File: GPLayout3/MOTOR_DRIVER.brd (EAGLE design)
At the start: 162.2 x 45.4 mm, 95 parts, among them T1 2N2222, T2 2N2222, U7 ATMEGA328P_TQFP, Y1 16MHz

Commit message: changed some drill sizes to .8 instead of .6. fixed some clearance issues with LED
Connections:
- removed net THERM2: LED2.THERMAL
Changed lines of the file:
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@@
 <?xml version="1.0" encoding="utf-8"?>
 <!DOCTYPE eagle SYSTEM "eagle.dtd">
-<eagle version="8.0.0">
+<eagle version="8.0.1">
 <drawing>
 <settings>
@@
 <setting verticaltext="up"/>
 </settings>
-<grid distance="6" unitdist="mil" unit="mil" style="lines" multiple="1" display="yes" altdistance="0.05" altunitdist="mm" altunit="mm"/>
+<grid distance="6" unitdist="mil" unit="mm" style="lines" multiple="1" display="yes" altdistance="0.05" altunitdist="mm" altunit="mm"/>
 <layers>
 <layer number="1" name="Top" color="4" fill="1" visible="yes" active="yes"/>
@@
 <wire x1="10.5" y1="25.25" x2="13.25" y2="25.25" width="2" layer="1"/>
 <wire x1="13.25" y1="25.25" x2="14.25" y2="26.25" width="2" layer="1"/>
-<via x="14.25" y="26.25" extent="1-16" drill="0.6"/>
+<via x="14.25" y="26.25" extent="1-16" drill="0.8"/>
 <wire x1="14.25" y1="26.25" x2="16.75" y2="26.25" width="2" layer="16"/>
 <wire x1="16.75" y1="26.25" x2="19.75" y2="29.25" width="2" layer="16"/>
-<via x="19.75" y="29.25" extent="1-16" drill="0.6"/>
+<via x="19.75" y="29.25" extent="1-16" drill="0.8"/>
 <wire x1="19.75" y1="29.25" x2="24.066" y2="29.25" width="2" layer="1"/>
 <wire x1="24.066" y1="29.25" x2="24.536" y2="29.72" width="2" layer="1"/>
@@
 <wire x1="3.166" y1="6.35" x2="3.166" y2="9.166" width="0.3048" layer="16"/>
 <wire x1="3.166" y1="9.166" x2="3.25" y2="9.25" width="0.3048" layer="16"/>
-<via x="3.25" y="9.25" extent="1-16" drill="0.6" diameter="0.6096"/>
+<via x="3.25" y="9.25" extent="1-16" drill="0.8" diameter="0.6096"/>
 <contactref element="SV5" pad="10"/>
 <contactref element="SV5" pad="9"/>
@@
 <contactref element="SV5" pad="7"/>
 <wire x1="3.166" y1="39.55" x2="7.125" y2="39.5" width="2" layer="1"/>
-<via x="7.125" y="39.5" extent="1-16" drill="0.6" shape="square"/>
+<via x="7.125" y="39.5" extent="1-16" drill="0.8" shape="square"/>
 <wire x1="7.125" y1="39.5" x2="29.75" y2="39.5" width="2" layer="16"/>
 <wire x1="29.75" y1="39.5" x2="29.81" y2="42.75" width="2" layer="16"/>
@@
 <wire x1="3.25" y1="22.5" x2="3.25" y2="23" width="2" layer="16"/>
 <wire x1="3.25" y1="23" x2="13.25" y2="23" width="2" layer="16"/>
-<via x="13.25" y="23" extent="1-16" drill="0.6"/>
+<via x="13.25" y="23" extent="1-16" drill="0.8"/>
 <wire x1="15" y1="23" x2="13.25" y2="23" width="2" layer="1"/>
 <wire x1="15.888" y1="23" x2="15" y2="23" width="0.8128" layer="1"/>
@@
 <wire x1="11.258" y1="29.112" x2="7.362" y2="29.112" width="2" layer="1"/>
 <wire x1="7.362" y1="29.112" x2="7.25" y2="29" width="2" layer="1"/>
-<via x="7.25" y="29" extent="1-16" drill="0.6"/>
+<via x="7.25" y="29" extent="1-16" drill="0.8"/>
 <wire x1="7.25" y1="26.252" x2="7.25" y2="29" width="2" layer="16"/>
 <wire x1="17.25" y1="6.25" x2="14.25" y2="6.25" width="0.6096" layer="1"/>
@@
 <wire x1="18.25" y1="25.5" x2="18.25" y2="20.25" width="2" layer="1"/>
 <wire x1="18.25" y1="20.25" x2="19.5" y2="20.25" width="2" layer="1"/>
-<via x="19.5" y="20.25" extent="1-16" drill="0.6"/>
+<via x="19.5" y="20.25" extent="1-16" drill="0.8"/>
 <wire x1="19.5" y1="20.25" x2="25.75" y2="20.25" width="2" layer="16"/>
-<via x="25.75" y="20.25" extent="1-16" drill="0.6"/>
+<via x="25.75" y="20.25" extent="1-16" drill="0.8"/>
 <wire x1="25.75" y1="20.25" x2="25.75" y2="17.594" width="2" layer="1"/>
 <wire x1="25.75" y1="17.594" x2="25.808" y2="17.536" width="2" layer="1"/>
@@
 <vertex x="161.5" y="7.5"/>
 </polygon>
-<contactref element="LED2" pad="THERMAL"/>
 <via x="157.045" y="3.425" extent="1-16" drill="0.381" diameter="0.05" shape="square"/>
 <via x="157.68" y="3.425" extent="1-16" drill="0.381" diameter="0.05" shape="square"/>
@@
 <via x="157.045" y="2.155" extent="1-16" drill="0.381" diameter="0.05" shape="square"/>
 <via x="157.68" y="2.155" extent="1-16" drill="0.381" diameter="0.05" shape="square"/>
-<via x="155.775" y="1.52" extent="1-16" drill="0.381" diameter="0.05" shape="square"/>
-<via x="156.41" y="1.52" extent="1-16" drill="0.381" diameter="0.05" shape="square"/>
+<via x="156.41" y="1.52" extent="1-16" drill="0.381" diameter="0.05"/>
 <via x="157.045" y="1.52" extent="1-16" drill="0.381" diameter="0.05" shape="square"/>
 <via x="157.68" y="1.52" extent="1-16" drill="0.381" diameter="0.05" shape="square"/>
-<via x="158.315" y="1.52" extent="1-16" drill="0.381" diameter="0.05" shape="square"/>
-<via x="158.95" y="1.52" extent="1-16" drill="0.381" diameter="0.05" shape="square"/>
+<via x="158.315" y="1.52" extent="1-16" drill="0.381" diameter="0.05"/>
 <via x="157.045" y="4.06" extent="1-16" drill="0.381" diameter="0.05" shape="square"/>
 <via x="157.68" y="4.06" extent="1-16" drill="0.381" diameter="0.05" shape="square"/>
@@
 <via x="157.68" y="5.33" extent="1-16" drill="0.381" diameter="0.05" shape="square"/>
 <via x="157.045" y="5.965" extent="1-16" drill="0.381" diameter="0.05" shape="square"/>
-<via x="156.41" y="5.965" extent="1-16" drill="0.381" diameter="0.05" shape="square"/>
-<via x="155.775" y="5.965" extent="1-16" drill="0.381" diameter="0.05" shape="square"/>
-<via x="158.315" y="5.965" extent="1-16" drill="0.381" diameter="0.05" shape="square"/>
-<via x="158.95" y="5.965" extent="1-16" drill="0.381" diameter="0.05" shape="square"/>
+<via x="156.41" y="5.965" extent="1-16" drill="0.381" diameter="0.05"/>
+<via x="158.315" y="5.965" extent="1-16" drill="0.381" diameter="0.05"/>
 <via x="157.695" y="5.965" extent="1-16" drill="0.381" diameter="0.05" shape="square"/>
 </signal>
@@
 <vertex x="161.5" y="38"/>
 </polygon>
-<via x="155.775" y="44.015" extent="1-16" drill="0.381" diameter="0.005" shape="square"/>
-<via x="156.41" y="44.015" extent="1-16" drill="0.381" diameter="0.005" shape="square"/>
+<via x="156.41" y="44.015" extent="1-16" drill="0.381" diameter="0.005"/>
 <via x="157.045" y="44.015" extent="1-16" drill="0.381" diameter="0.005" shape="square"/>
 <via x="157.68" y="44.015" extent="1-16" drill="0.381" diameter="0.005" shape="square"/>
-<via x="158.315" y="44.015" extent="1-16" drill="0.381" diameter="0.005" shape="square"/>
-<via x="158.95" y="44.015" extent="1-16" drill="0.381" diameter="0.005" shape="square"/>
+<via x="158.315" y="44.015" extent="1-16" drill="0.381" diameter="0.005"/>
 <via x="157.045" y="43.38" extent="1-16" drill="0.381" diameter="0.005" shape="square"/>
 <via x="157.68" y="43.38" extent="1-16" drill="0.381" diameter="0.005" shape="square"/>
@@
 <via x="157.045" y="40.205" extent="1-16" drill="0.381" diameter="0.005" shape="square"/>
 <via x="157.68" y="40.205" extent="1-16" drill="0.381" diameter="0.005" shape="square"/>
-<via x="155.775" y="39.57" extent="1-16" drill="0.381" diameter="0.005" shape="square"/>
-<via x="156.41" y="39.57" extent="1-16" drill="0.381" diameter="0.005" shape="square"/>
+<via x="156.41" y="39.57" extent="1-16" drill="0.381" diameter="0.005"/>
 <via x="157.045" y="39.57" extent="1-16" drill="0.381" diameter="0.005" shape="square"/>
 <via x="157.68" y="39.57" extent="1-16" drill="0.381" diameter="0.005" shape="square"/>
-<via x="158.315" y="39.57" extent="1-16" drill="0.381" diameter="0.005" shape="square"/>
-<via x="158.95" y="39.57" extent="1-16" drill="0.381" diameter="0.005" shape="square"/>
+<via x="158.315" y="39.57" extent="1-16" drill="0.381" diameter="0.005"/>
 <polygon width="0.4064" layer="1">
 <vertex x="153.5" y="45"/>

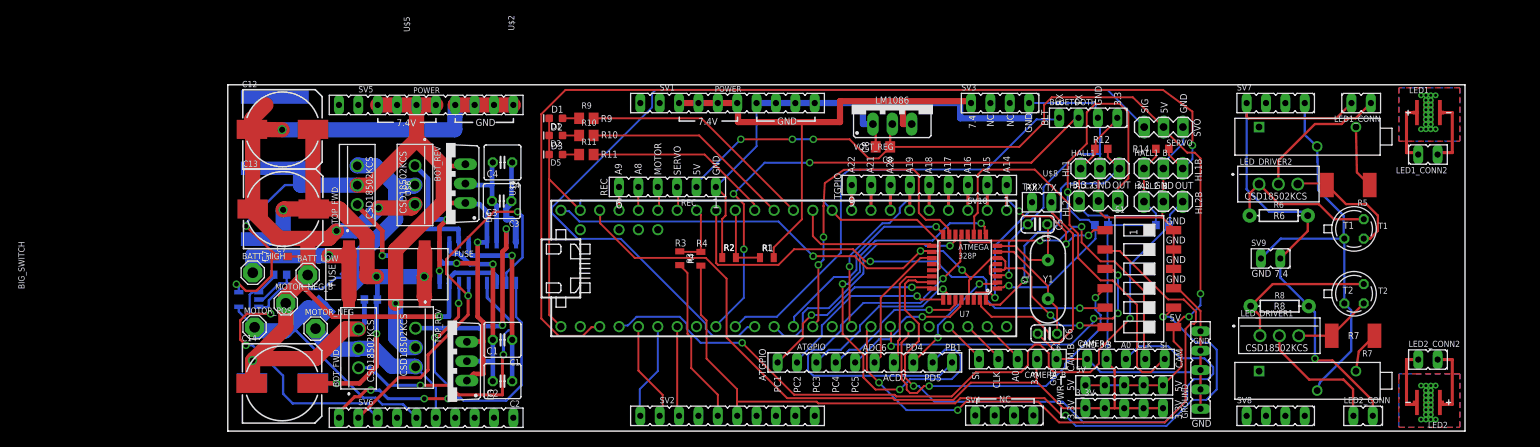
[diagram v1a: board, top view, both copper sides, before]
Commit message: larger pad for LEDs
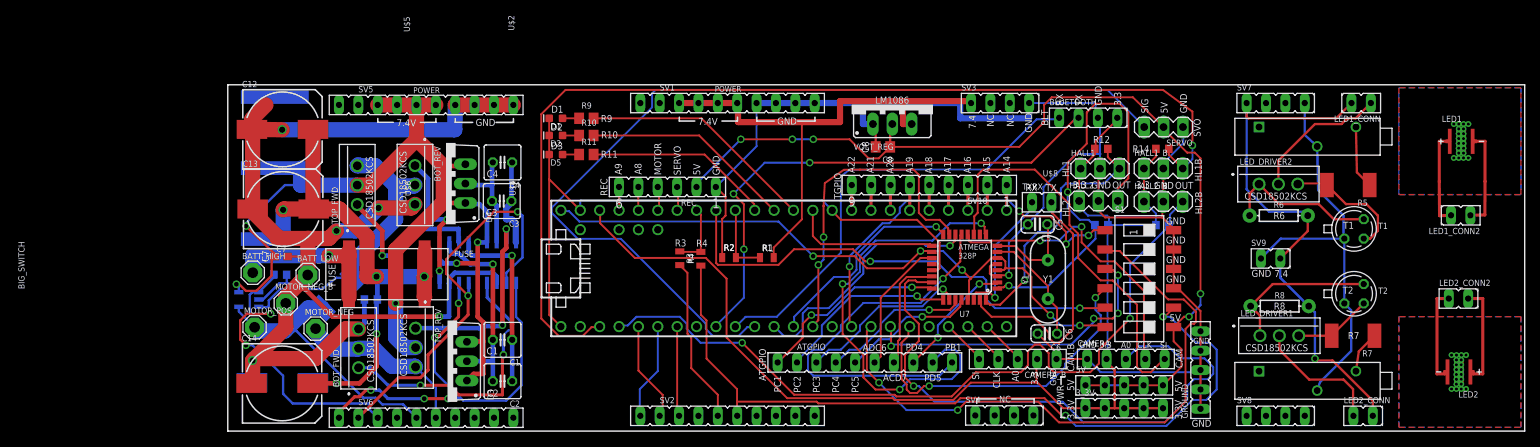
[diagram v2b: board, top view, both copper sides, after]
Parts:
- moved LED1_CONN2 9.05 mm to (157.8, 28.3)
- moved LED2_CONN2 8.94 mm to (165.1, 17.4)
- moved LED1 5.71 mm to (161.7, 38.0)
- moved LED2 5.66 mm to (161.4, 7.75)
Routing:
- net LED1LO: track 9.04 -> 13.2 mm
- net LED2LO: track 8.69 -> 12.7 mm
- net LED1HI: track 8.66 -> 12.6 mm
- net LED2HI: track 9.96 -> 13.3 mm
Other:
- board size 162.2 x 45.4 mm -> 170 x 45.4 mm
